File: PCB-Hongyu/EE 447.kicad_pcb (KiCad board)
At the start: 4 copper layers, 109.5 x 100 mm, 74 parts, among them J1 Conn_01x04_Pin, J2 FH34SRJ-24S-0.5SH_99_, J3 S2B-PH-SM4-TB, J4 Conn_01x01_Pin, J5 Conn_01x02_Pin, J6 Conn_01x01_Pin, J7 Conn_01x01_Pin, J8 Conn_01x02_Pin, J9 61302421121, Q1 BSS138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

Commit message: MCB
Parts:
- added H1: MountingHole, MountingHole:MountingHole_3.2mm_M3, F.Cu at (190.1, 109.2)
- added H2: MountingHole, MountingHole:MountingHole_3.2mm_M3, F.Cu at (234.9, 109.2)
- added H3: MountingHole, MountingHole:MountingHole_3.2mm_M3, F.Cu at (234.9, 196.8)
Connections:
- net Net-(R3-Pad2) renamed /Epaper/EPD_PWR
- C7 pad 2: Net-(C7-Pad2) -> /Epaper/3V3_OUT
- L1 pad 1: Net-(C7-Pad2) -> /Epaper/3V3_OUT
- U1 pad 11: unconnected-(U1-*PENIRQ-Pad11) -> /PENIRQ
- U2 pad 20: unconnected-(U2-IO9-Pad20) -> /PENIRQ
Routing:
- net /PENIRQ: track 0.00 -> 36.5 mm
- net +BATT: track 124.7 -> 142.7 mm, vias 1 -> 2
- net EPD_CS: track 79.6 -> 67.2 mm
- net GND: track 93.9 -> 89.9 mm, vias 218 -> 228
- net CLK: track 80.1 -> 83.2 mm
- net Net-(C7-Pad2): track 2.05 -> 0.00 mm
- net /Epaper/3V3_OUT: track 21.6 -> 23.6 mm
- net MISO: track 61.5 -> 60.4 mm
- net MOSI: track 100.0 -> 100.6 mm
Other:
- board size 109.5 x 100 mm -> 55.9 x 100 mm

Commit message: footprint
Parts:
- added L1: WE-MXGI_5030, Custom:WE-MXGI_5030, F.Cu at (276.0, 127.9)
- C1, C2, C3, C5: value ~ -> NC
- C17: value 104 -> 0.1u
- C4: value 10 uF -> 10u
- C6: value 0.1 uF -> 0.1u
- L2: value 3.3 uH -> 3.3uH
- R2, R4: value 10K -> 10k
- R3, R5: value 47K -> 47k
- R6: value 100K -> 100k
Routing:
- net GND: track 89.9 -> 202.9 mm, vias 228 -> 413
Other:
- board size 55.9 x 100 mm -> 57.4 x 100 mm

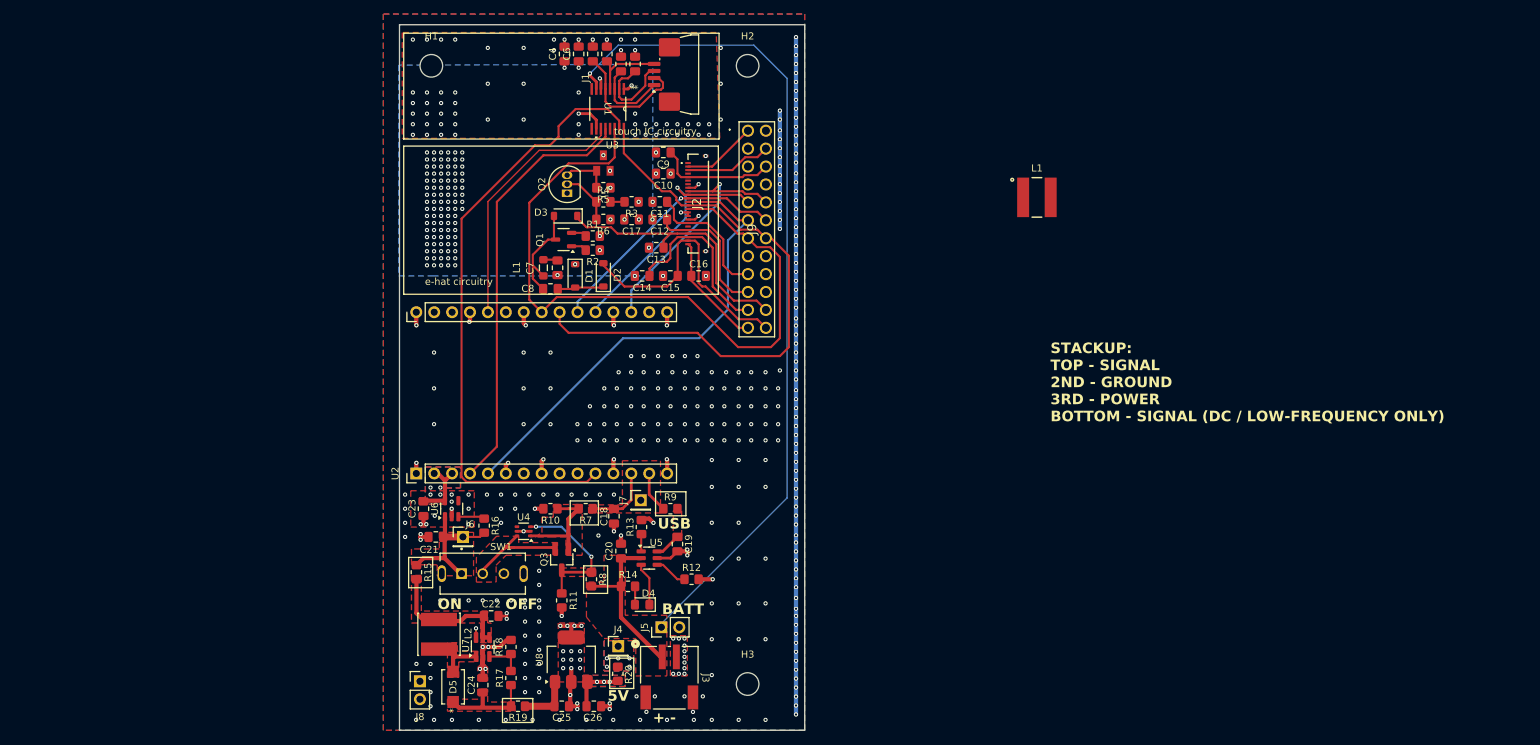
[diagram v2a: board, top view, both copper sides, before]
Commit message: added power digikey links
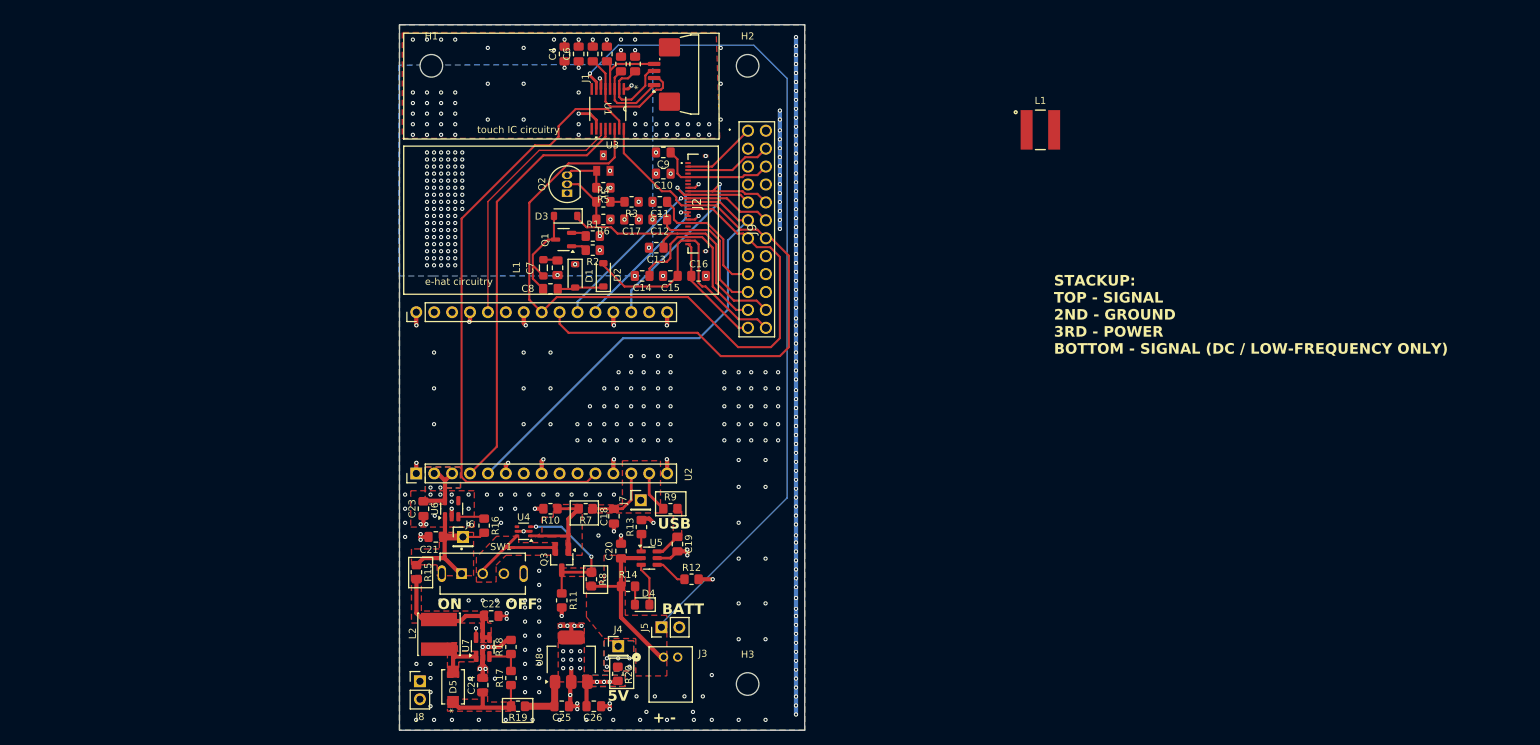
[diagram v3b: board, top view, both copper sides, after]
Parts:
- J3: value S2B-PH-SM4-TB -> S2B-PH-K-SLFSN; footprint Library:CONN_S2B-PH-SM4-TB_JST -> Library:CONN_S2B-PH-K-S_JST
- moved L1 9.59 mm to (276.4, 118.3)
- moved J3 3.02 mm to (223.0, 193.0)
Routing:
- net GND: vias 413 -> 381

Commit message: added some stuff
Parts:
- C1, C2, C3, C5: footprint Capacitor_SMD:C_0805_2012Metric_Pad1.18x1.45mm_HandSolder -> Capacitor_SMD:C_0603_1608Metric_Pad1.08x0.95mm_HandSolder
- L1: value 10u -> WE-MXGI_5030

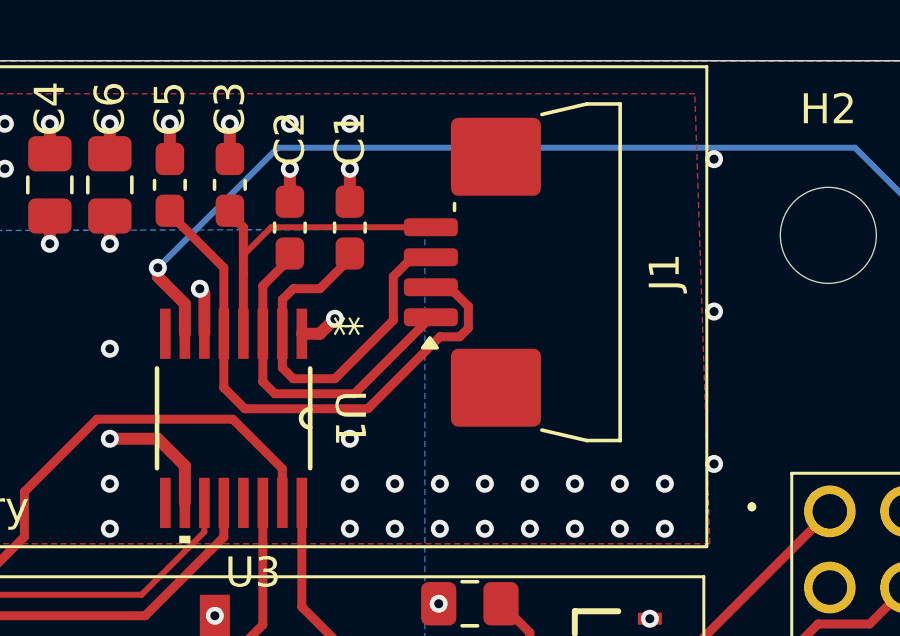
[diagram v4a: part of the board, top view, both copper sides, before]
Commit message: finished adding parts and fixing silkscreen
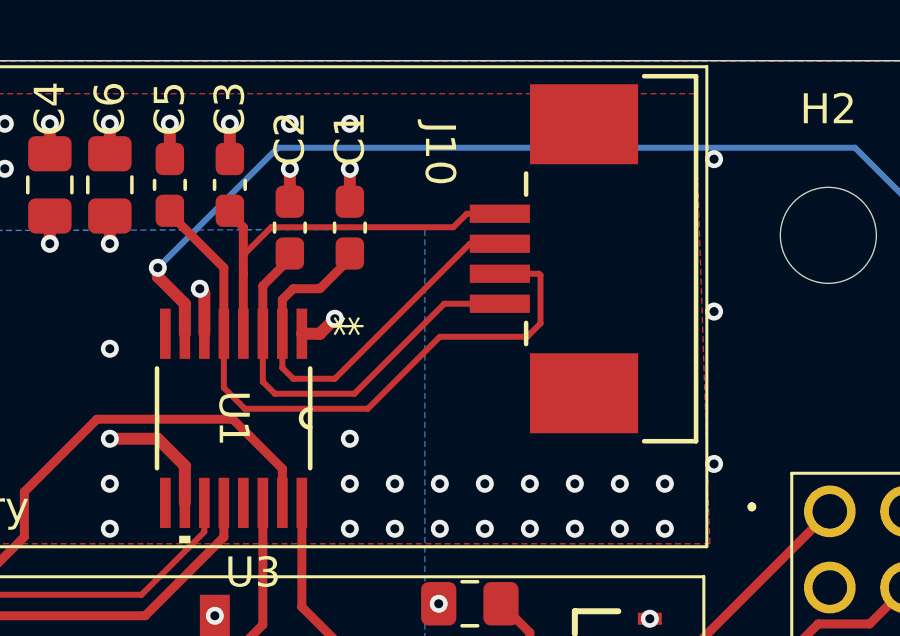
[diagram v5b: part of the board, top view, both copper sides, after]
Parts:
- removed J1: Conn_01x04_Pin, Connector_FFC-FPC:JUSHUO_AFA07-S04FCA-00_1x4-1MP_P1.0mm_Horizontal
- added J10: 84952-4, Hongyu:CON4_SMT-RA_FCC-FPC2, F.Cu at (226.7, 110.0)
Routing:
- net Net-(U1-Y-): track 18.3 -> 21.5 mm
- net Net-(U1-Y+): track 11.3 -> 13.8 mm
- net Net-(U1-X-): track 11.4 -> 13.9 mm
- net Net-(U1-X+): track 12.7 -> 14.4 mm

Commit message: i try edit stuff but NOT LET ME SYMbOL so i say claire do it hehe ty
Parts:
- removed the L1 at (206.0, 137.8)
- moved L1 76.6 mm to (202.0, 136.5), turned to 90 degrees
- moved C13 1.00 mm to (221.0, 135.0)
- moved Q2 0.36 mm to (209.0, 127.3)
- moved D3 0.30 mm to (208.8, 130.5)
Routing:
- net /Epaper/3V3_OUT: track 23.6 -> 49.4 mm
- net Net-(D3-A): track 15.1 -> 26.4 mm
- net MOSI: track 100.5 -> 109.2 mm
- net MISO: track 60.4 -> 63.2 mm
- net /PENIRQ: track 36.5 -> 38.3 mm
- net +BATT: vias 2 -> 1

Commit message: footprint pull push
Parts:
- removed D1, D2, D3: MBR0530, Diode_SMD:D_SOD-123
- added CR1: SS0530_R1_00001, Library:SOD-123_PNJ, F.Cu at (172.7, 131.9)
- added CR2: SS0530_R1_00001, Library:SOD-123_PNJ, F.Cu at (172.7, 135.4)
- added CR3: SS0530_R1_00001, Library:SOD-123_PNJ, F.Cu at (172.7, 138.8)
- R1: value 3 -> 0.47

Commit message: eieio i think i done
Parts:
- moved CR2 41.9 mm to (214.5, 139.0), turned to 90 degrees
- moved CR3 37.8 mm to (210.5, 139.0), turned to -90 degrees
- moved CR1 35.8 mm to (208.5, 130.5), turned to 180 degrees
